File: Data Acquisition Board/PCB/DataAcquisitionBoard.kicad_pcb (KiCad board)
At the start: 2 copper layers, 99.1 x 68.6 mm, 14 parts, among them P1 BNC, P2 BNC, P3 BNC, P4 BNC, P5 CONN_01X04

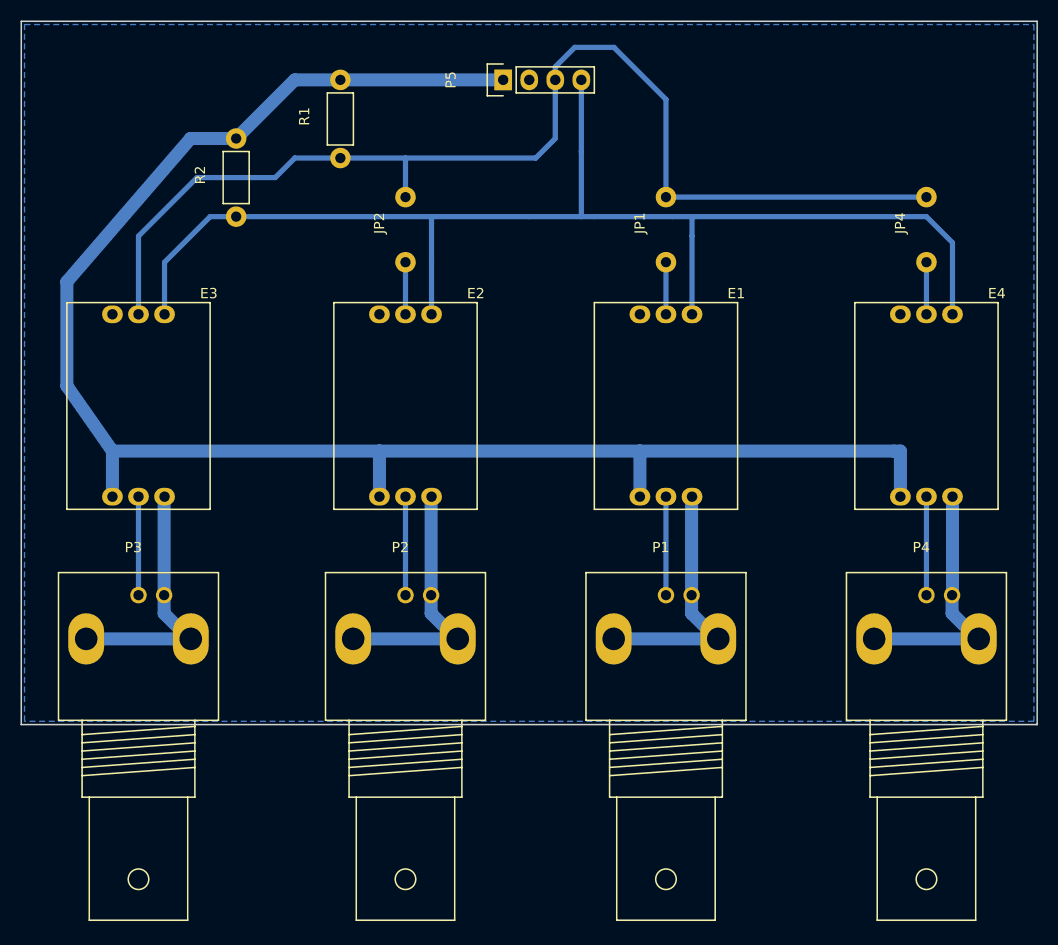
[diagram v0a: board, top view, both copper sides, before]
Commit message: Updated PCB to allow for chaining of multiple boards
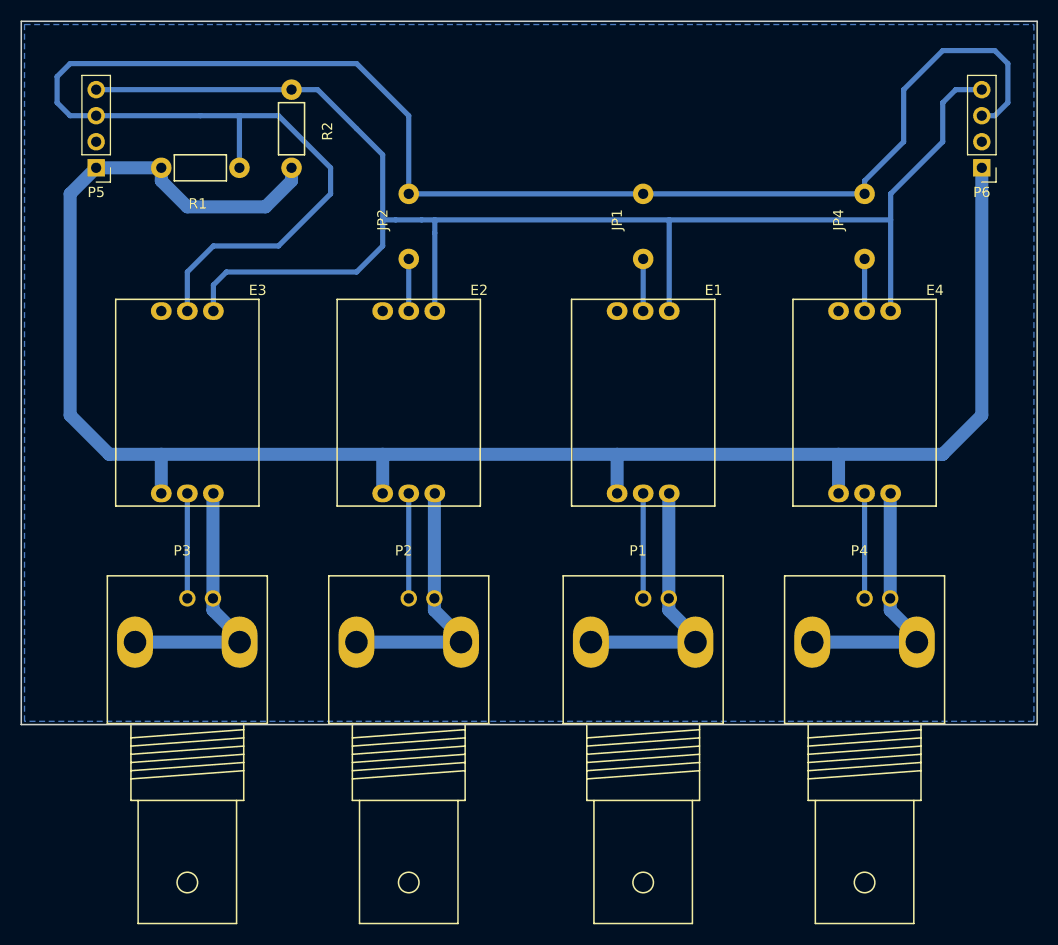
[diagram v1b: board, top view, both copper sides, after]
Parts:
- added P6: CONN_01X04, Pin_Headers:Pin_Header_Straight_1x04_Pitch2.54mm, F.Cu at (160.0, 104.1)
- P5: footprint Pin_Headers:Pin_Header_Straight_1x04 -> Pin_Headers:Pin_Header_Straight_1x04_Pitch2.54mm
- R1: value 11K -> 12K
- R2: value 10K -> 12K
- moved P5 40.6 mm to (73.7, 104.1), turned to 180 degrees
- moved R2 13.5 mm to (92.7, 96.5), turned to 270 degrees
- moved R1 9.89 mm to (87.6, 104.1), turned to 180 degrees
- moved E4 6.04 mm to (148.6, 127.0)
- moved JP4 6.04 mm to (148.6, 113.0)
- moved P4 6.04 mm to (148.6, 151.1)
- moved E3 4.77 mm to (82.5, 127.0)
- moved P3 4.77 mm to (82.5, 151.1)
- moved E1 2.25 mm to (127.0, 127.0)
- moved JP1 2.25 mm to (127.0, 113.0)
- moved P1 2.25 mm to (127.0, 151.1)
- moved E2 0.45 mm to (104.1, 127.0)
- moved JP2 0.45 mm to (104.1, 113.0)
- moved P2 0.45 mm to (104.1, 151.1)
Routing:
- net A4: track 111.6 -> 180.3 mm
- net A5: track 124.2 -> 154.2 mm
- net +5V: track 163.8 -> 180.3 mm
- net Net-(E4-Pad5): track 9.60 -> 10.2 mm
- net Net-(E3-Pad5): track 9.60 -> 10.2 mm
- net Net-(E2-Pad5): track 9.60 -> 10.2 mm
- net Net-(E1-Pad5): track 9.60 -> 10.2 mm
- net Net-(E4-Pad4): track 25.3 -> 25.8 mm
- net Net-(E1-Pad4): track 25.3 -> 25.8 mm
- net Net-(E2-Pad4): track 25.3 -> 25.8 mm
